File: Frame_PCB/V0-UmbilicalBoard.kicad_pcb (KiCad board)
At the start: 2 copper layers, 122 x 37 mm, 17 parts, among them J10 Neopixel Strip 1, J11 Neopixel Strip 1, J12 Neopixel Out, J13 Conn_02x08_Top_Bottom, J14 Conn_01x03, J2 Motor, J3 Hotend Fan, J4 Part Cooling Fan, J5 Heater, J6 Thermistor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

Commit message: changed hotend fan silkscreen lettering
+ and - were swapped unintentionally
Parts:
- renumbered J14 to Klicky1
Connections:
- net Net-(J13-Pad12) renamed /KlickySignal
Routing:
- net /A2: track 31.3 -> 30.1 mm
- net Net-(J8-Pad1): track 42.7 -> 41.6 mm
- net /B2: track 43.5 -> 42.7 mm
- net /Hotend_Fan+: track 24.4 -> 23.7 mm
- net /B1: track 37.3 -> 38.0 mm
- net DataIn2: track 120.0 -> 120.5 mm
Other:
- net class Motor_traces added: clearance 0.35, trace_width 1, via_dia 0.8, via_drill 0.4
- board text added: "JLCJLCJLCJLC"

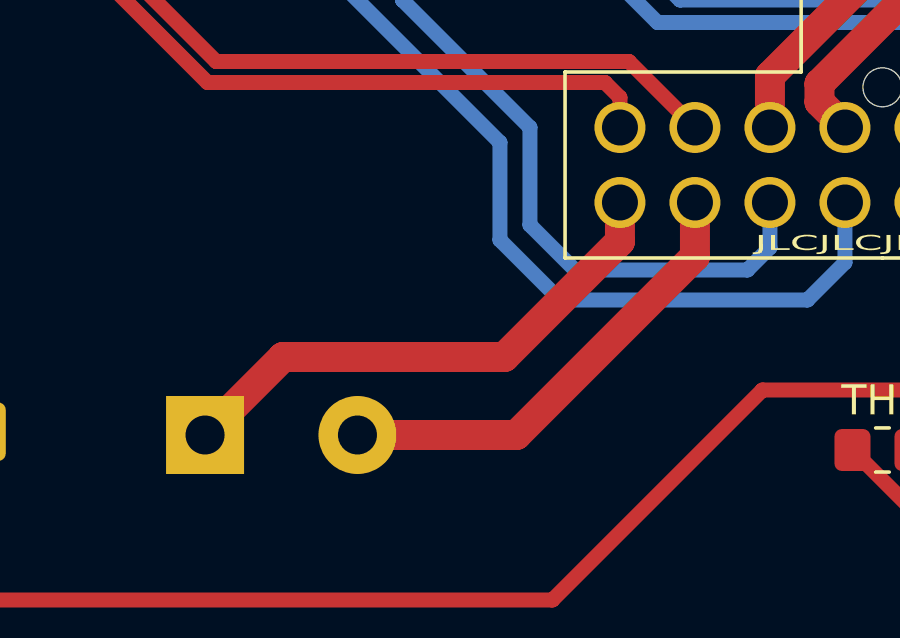
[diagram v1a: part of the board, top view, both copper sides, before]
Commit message: uploaded STLs
STLs for toolhead spacers and frame PCB cover.
FramePCBCover_topHole.stl features a hole in the cover to solder a 3-pin JST-XH on the opposite side for routing a servo cable to the print chamber (i.e. nozzle wiper arm mechanism)
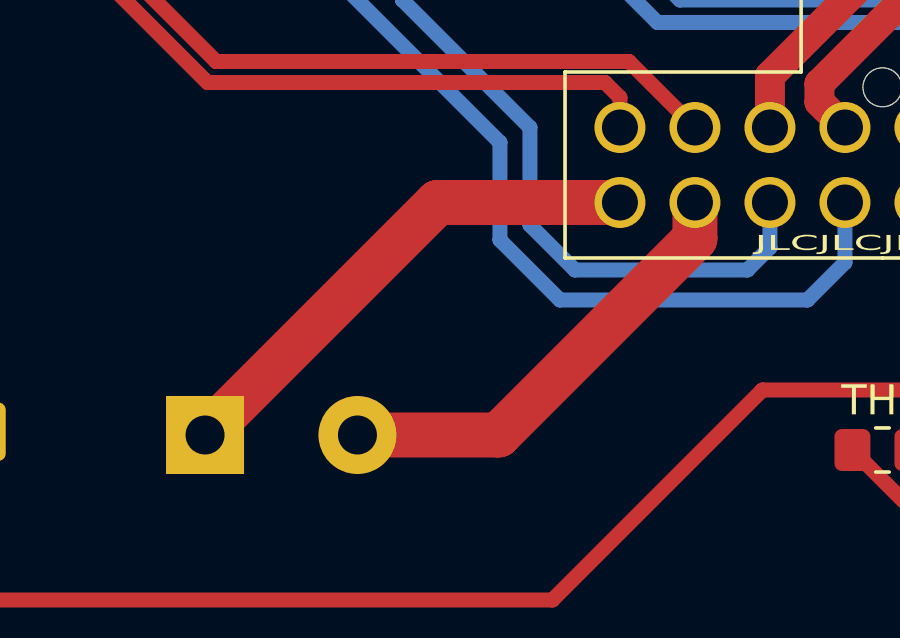
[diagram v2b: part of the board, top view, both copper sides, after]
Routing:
- net Net-(J13-Pad16): track 17.8 -> 17.0 mm
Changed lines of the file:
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@@
     (thickness 1.6)
     (drawings 70)
-    (tracks 114)
+    (tracks 112)
     (zones 0)
     (modules 17)
@@
   (page A4)
   (layers
-    (0 F.Cu signal hide)
+    (0 F.Cu signal)
     (31 B.Cu signal)
     (32 B.Adhes user)
@@
     (user_trace_width 0.5)
     (user_trace_width 1)
+    (user_trace_width 1.5)
     (trace_clearance 0.2)
     (zone_clearance 0.508)
@@
   (segment (start 69.928 104.472) (end 69.928 108.89) (width 0.5) (layer B.Cu) (net 15))
   (segment (start 61.706 96.25) (end 69.928 104.472) (width 0.5) (layer B.Cu) (net 15))
-  (segment (start 77.42 109) (end 80.02 106.4) (width 1) (layer F.Cu) (net 16))
-  (segment (start 80.02 106.4) (end 87.4 106.4) (width 1) (layer F.Cu) (net 16))
-  (segment (start 91.25 102.55) (end 91.25 101.25) (width 1) (layer F.Cu) (net 16))
-  (segment (start 87.4 106.4) (end 91.25 102.55) (width 1) (layer F.Cu) (net 16))
-  (segment (start 82.5 109) (end 87.8 109) (width 1) (layer F.Cu) (net 17))
-  (segment (start 93.75 103.05) (end 93.75 101.25) (width 1) (layer F.Cu) (net 17))
-  (segment (start 87.8 109) (end 93.75 103.05) (width 1) (layer F.Cu) (net 17))
+  (segment (start 85.17 101.25) (end 91.25 101.25) (width 1.5) (layer F.Cu) (net 16))
+  (segment (start 77.42 109) (end 85.17 101.25) (width 1.5) (layer F.Cu) (net 16))
+  (segment (start 93.75 102.452081) (end 93.75 101.25) (width 1.5) (layer F.Cu) (net 17))
+  (segment (start 87.202081 109) (end 93.75 102.452081) (width 1.5) (layer F.Cu) (net 17))
+  (segment (start 82.5 109) (end 87.202081 109) (width 1.5) (layer F.Cu) (net 17))
   (segment (start 65 91.11) (end 67.11 89) (width 0.5) (layer B.Cu) (net 18))
   (segment (start 67.11 89) (end 86.25 89) (width 0.5) (layer B.Cu) (net 18))
@@
   (segment (start 110.75 99.25) (end 108.75 101.25) (width 0.5) (layer B.Cu) (net 20))
   (segment (start 110.75 97.25) (end 110.75 99.25) (width 0.5) (layer B.Cu) (net 20))
+  (segment (start 107.5 109) (end 107.5 105) (width 0.5) (layer F.Cu) (net 21))
+  (segment (start 106.25 103.75) (end 106.25 101.25) (width 0.5) (layer F.Cu) (net 21))
+  (segment (start 107.5 105) (end 106.25 103.75) (width 0.5) (layer F.Cu) (net 21))
   (segment (start 101.25 101.25) (end 101.25 106.5) (width 0.5) (layer B.Cu) (net 22))
   (segment (start 101.25 106.5) (end 102.25 107.5) (width 0.5) (layer B.Cu) (net 22))
   (segment (start 108.5 107.5) (end 110 109) (width 0.5) (layer B.Cu) (net 22))
   (segment (start 102.25 107.5) (end 108.5 107.5) (width 0.5) (layer B.Cu) (net 22))
-  (segment (start 107.5 109) (end 107.5 105) (width 0.5) (layer F.Cu) (net 21))
-  (segment (start 106.25 103.75) (end 106.25 101.25) (width 0.5) (layer F.Cu) (net 21))
-  (segment (start 107.5 105) (end 106.25 103.75) (width 0.5) (layer F.Cu) (net 21))
   (zone (net 12) (net_name 5V) (layer F.Cu) (hatch edge 0.508)
     (connect_pads (clearance 0.508))
